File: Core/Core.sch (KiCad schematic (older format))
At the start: 12 parts, among them U10 TL072, U11 TL072, U12 TL072, U13 TL072, U2 DG408, U3 DG408, U4 DG408, U5 DG408, U6 DG408, U7 DG408, U8 DG408, U9 DG408

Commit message: Update termination
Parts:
- U2, U3, U4, U5, U6, U7, U8, U9: symbol MIDI_Tangle-rescue:DG408-Custom -> CustomLib:DG408
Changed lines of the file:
@@
 $EndDescr
 $Comp
-L MIDI_Tangle-rescue:DG408-Custom U?
+L CustomLib:DG408 U?
 U 1 1 6041C336
 P 3000 1900
@@
 	3550 1900 3500 1900
 $Comp
-L MIDI_Tangle-rescue:DG408-Custom U?
+L CustomLib:DG408 U?
 U 1 1 60465DBA
 P 3050 4000
@@
 	3600 4000 3550 4000
 $Comp
-L MIDI_Tangle-rescue:DG408-Custom U?
+L CustomLib:DG408 U?
 U 1 1 6046F2FE
 P 3100 6100
@@
 	3650 6100 3600 6100
 $Comp
-L MIDI_Tangle-rescue:DG408-Custom U?
+L CustomLib:DG408 U?
 U 1 1 60472B23
 P 5050 1900
@@
 	5600 1900 5550 1900
 $Comp
-L MIDI_Tangle-rescue:DG408-Custom U?
+L CustomLib:DG408 U?
 U 1 1 60472B5F
 P 5100 4000
@@
 	5650 4000 5600 4000
 $Comp
-L MIDI_Tangle-rescue:DG408-Custom U?
+L CustomLib:DG408 U?
 U 1 1 60472B9B
 P 5150 6100
@@
 	5700 6100 5650 6100
 $Comp
-L MIDI_Tangle-rescue:DG408-Custom U?
+L CustomLib:DG408 U?
 U 1 1 60488951
 P 7350 1950
@@
 	7900 1950 7850 1950
 $Comp
-L MIDI_Tangle-rescue:DG408-Custom U?
+L CustomLib:DG408 U?
 U 1 1 6048898D
 P 7400 4050

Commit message: Add custom footprints and symbols
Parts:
- U2, U3, U4, U5, U6, U7, U8, U9: symbol CustomLib:DG408 -> Custom_Sym:DG408
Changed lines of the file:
@@
 $EndDescr
 $Comp
-L CustomLib:DG408 U?
+L Custom_Sym:DG408 U?
 U 1 1 6041C336
 P 3000 1900
@@
 	3550 1900 3500 1900
 $Comp
-L CustomLib:DG408 U?
+L Custom_Sym:DG408 U?
 U 1 1 60465DBA
 P 3050 4000
@@
 	3600 4000 3550 4000
 $Comp
-L CustomLib:DG408 U?
+L Custom_Sym:DG408 U?
 U 1 1 6046F2FE
 P 3100 6100
@@
 	3650 6100 3600 6100
 $Comp
-L CustomLib:DG408 U?
+L Custom_Sym:DG408 U?
 U 1 1 60472B23
 P 5050 1900
@@
 	5600 1900 5550 1900
 $Comp
-L CustomLib:DG408 U?
+L Custom_Sym:DG408 U?
 U 1 1 60472B5F
 P 5100 4000
@@
 	5650 4000 5600 4000
 $Comp
-L CustomLib:DG408 U?
+L Custom_Sym:DG408 U?
 U 1 1 60472B9B
 P 5150 6100
@@
 	5700 6100 5650 6100
 $Comp
-L CustomLib:DG408 U?
+L Custom_Sym:DG408 U?
 U 1 1 60488951
 P 7350 1950
@@
 	7900 1950 7850 1950
 $Comp
-L CustomLib:DG408 U?
+L Custom_Sym:DG408 U?
 U 1 1 6048898D
 P 7400 4050

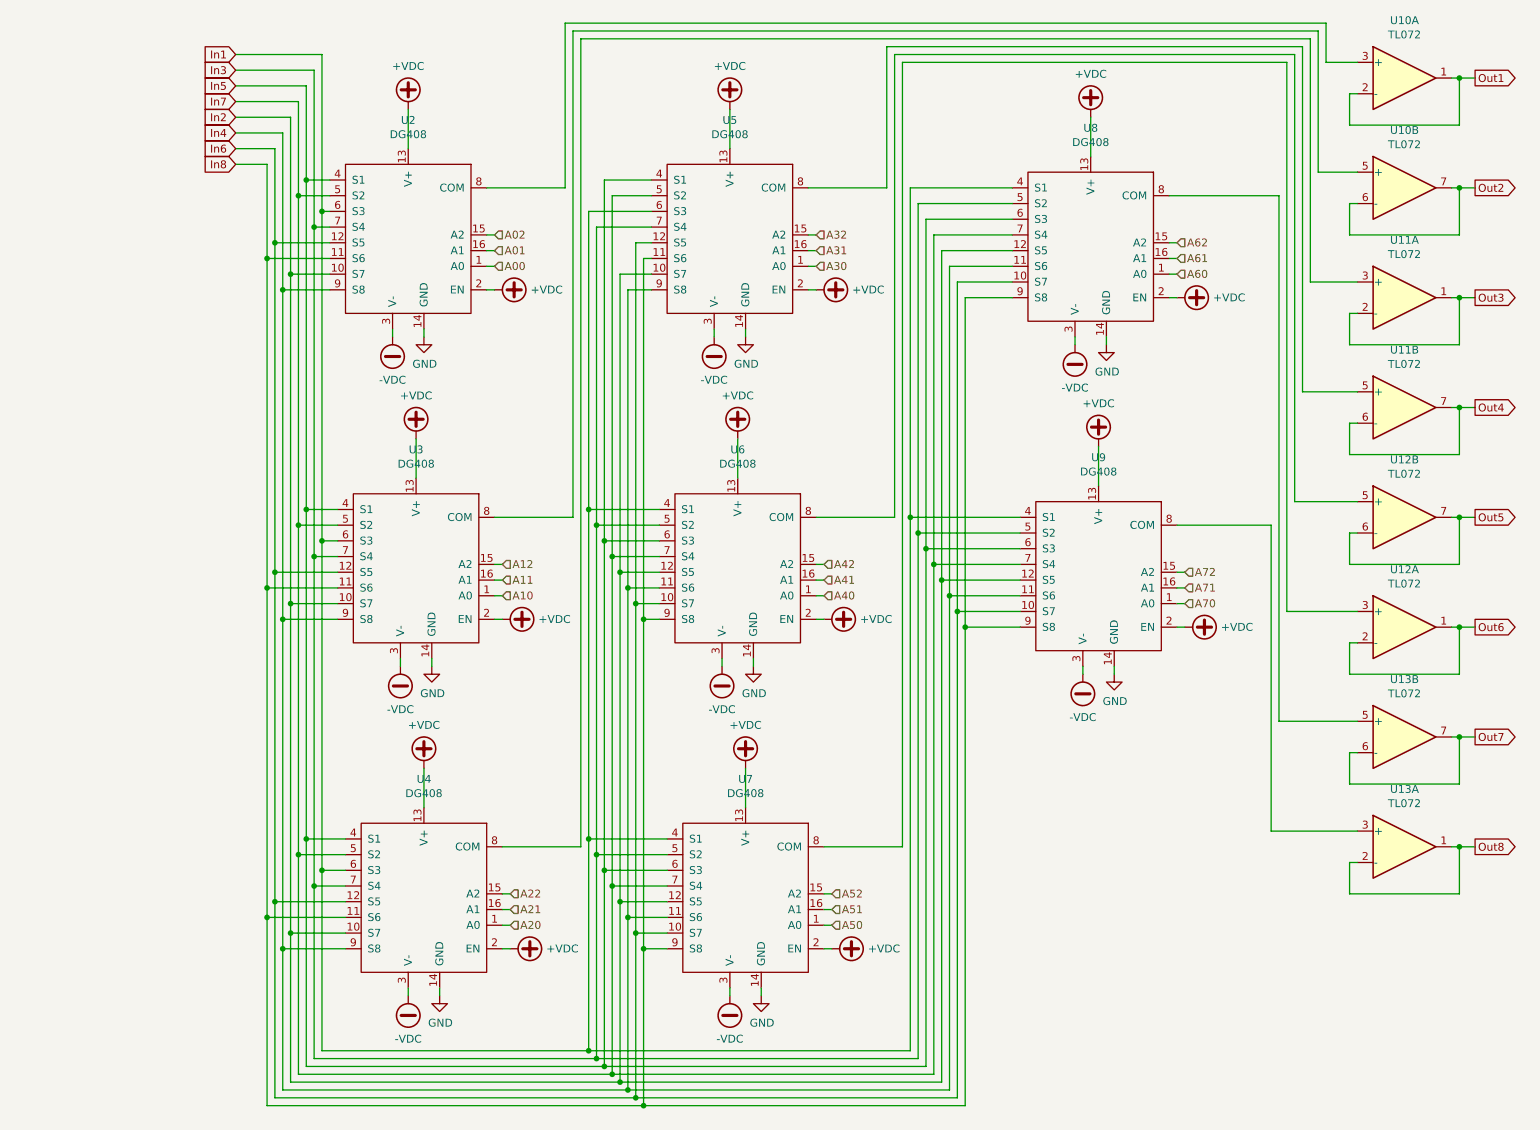
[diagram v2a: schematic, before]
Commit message: Add shift-registers+++
Added shift-registers
Added power protection
Changed USB footprint
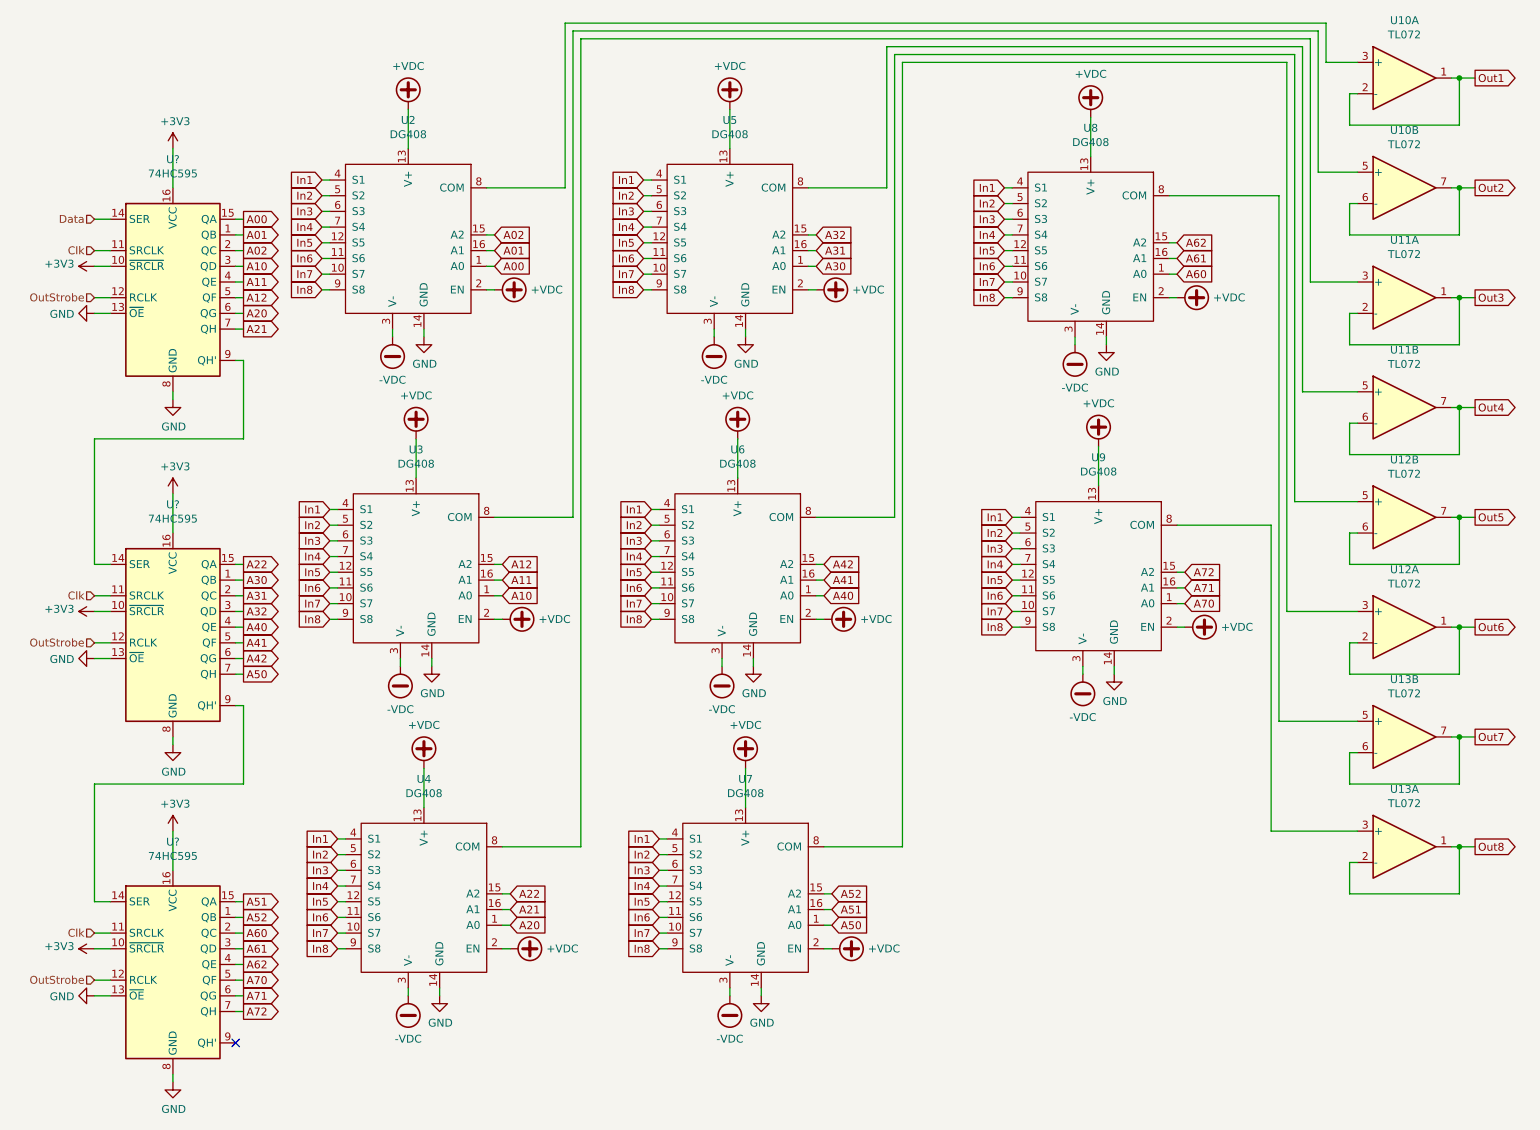
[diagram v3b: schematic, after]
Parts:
- added U? (x3): 74HC595, Package_SO:SO-16_3.9x9.9mm_P1.27mm, symbol 74xx:74HC595
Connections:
- net A00: now also U?.15 (QA)
- net A01: now also U?.1 (QB)
- net A02: now also U?.2 (QC)
- net A10: now also U?.3 (QD)
- net A11: now also U?.4 (QE)
- net A12: now also U?.5 (QF)
- net A20: now also U?.6 (QG)
- net A21: now also U?.7 (QH)
- net A22: now also U?.15 (QA)
- net A30: now also U?.1 (QB)
- net A31: now also U?.2 (QC)
- net A32: now also U?.3 (QD)
- net A40: now also U?.4 (QE)
- net A41: now also U?.5 (QF)
- net A42: now also U?.6 (QG)
- net A50: now also U?.7 (QH)
- net A51: now also U?.15 (QA)
- net A52: now also U?.1 (QB)
- net A60: now also U?.2 (QC)
- net A61: now also U?.3 (QD)
- net A62: now also U?.4 (QE)
- net A70: now also U?.5 (QF)
- net A71: now also U?.6 (QG)
- net A72: now also U?.7 (QH)
- net GND: now also U?.13 (~OE), U?.13 (~OE), U?.13 (~OE), U?.8 (GND), U?.8 (GND), U?.8 (GND)
- net In1: now also U2.4 (S1), U3.4 (S1), U4.4 (S1), U5.4 (S1); no longer U2.6 (S3), U3.6 (S3), U4.6 (S3), U5.6 (S3)
- net In2: now also U2.5 (S2), U3.5 (S2), U4.5 (S2), U5.5 (S2), U6.5 (S2), U7.5 (S2), U8.5 (S2), U9.5 (S2); no longer U2.10 (S7), U3.10 (S7), U4.10 (S7), U5.10 (S7), U6.12 (S5), U7.12 (S5), U8.12 (S5), U9.12 (S5)
- net In3: now also U2.6 (S3), U3.6 (S3), U4.6 (S3), U5.6 (S3), U6.6 (S3), U7.6 (S3), U8.6 (S3), U9.6 (S3); no longer U2.7 (S4), U3.7 (S4), U4.7 (S4), U5.7 (S4), U6.5 (S2), U7.5 (S2), U8.5 (S2), U9.5 (S2)
- net In4: now also U2.7 (S4), U3.7 (S4), U4.7 (S4), U5.7 (S4), U6.7 (S4), U7.7 (S4), U8.7 (S4), U9.7 (S4); no longer U2.9 (S8), U3.9 (S8), U4.9 (S8), U5.9 (S8), U6.11 (S6), U7.11 (S6), U8.11 (S6), U9.11 (S6)
- net In5: now also U2.12 (S5), U3.12 (S5), U4.12 (S5), U5.12 (S5), U6.12 (S5), U7.12 (S5), U8.12 (S5), U9.12 (S5); no longer U2.4 (S1), U3.4 (S1), U4.4 (S1), U5.4 (S1), U6.6 (S3), U7.6 (S3), U8.6 (S3), U9.6 (S3)
- net In6: now also U2.11 (S6), U3.11 (S6), U4.11 (S6), U5.11 (S6), U6.11 (S6), U7.11 (S6), U8.11 (S6), U9.11 (S6); no longer U2.12 (S5), U3.12 (S5), U4.12 (S5), U5.12 (S5), U6.10 (S7), U7.10 (S7), U8.10 (S7), U9.10 (S7)
- net In7: now also U2.10 (S7), U3.10 (S7), U4.10 (S7), U5.10 (S7), U6.10 (S7), U7.10 (S7), U8.10 (S7), U9.10 (S7); no longer U2.5 (S2), U3.5 (S2), U4.5 (S2), U5.5 (S2), U6.7 (S4), U7.7 (S4), U8.7 (S4), U9.7 (S4)
- net In8: now also U2.9 (S8), U3.9 (S8), U4.9 (S8), U5.9 (S8); no longer U2.11 (S6), U3.11 (S6), U4.11 (S6), U5.11 (S6)
- new net: U?.14 (SER), U?.9 (QH') (x2)
- new net +3V3: U?.10 (~SRCLR), U?.10 (~SRCLR), U?.10 (~SRCLR), U?.16 (VCC), U?.16 (VCC), U?.16 (VCC)
- new net Clk: U?.11 (SRCLK), U?.11 (SRCLK), U?.11 (SRCLK)
- new net Data: U?.14 (SER)
- new net OutStrobe: U?.12 (RCLK), U?.12 (RCLK), U?.12 (RCLK)
- no-connect marks 0 -> 1
